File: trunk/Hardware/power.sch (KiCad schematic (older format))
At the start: 131 parts, among them Q1 SI1403, Q2 SI1403, Q3 SI1403, Q4 SI1403, Q5 SI1403, U24 TLV61220, U25 TLV61220, U26 TLV61220, U27 LM3671, U28 DS2710

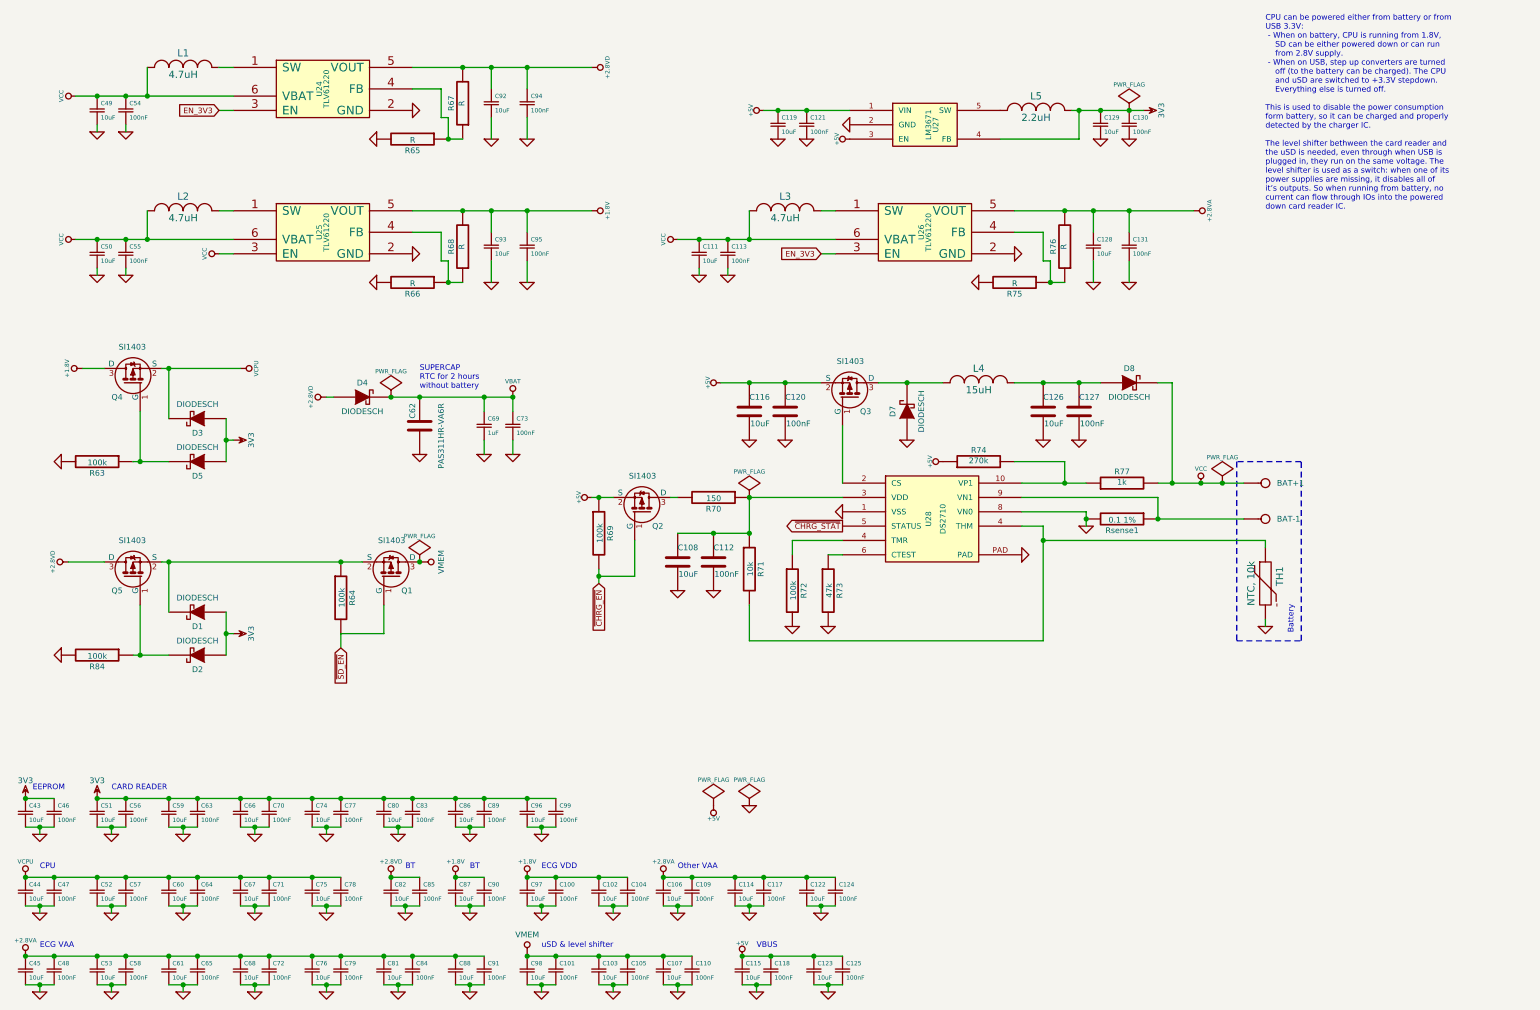
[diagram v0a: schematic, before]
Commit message: Fix even more typos, arrange parts in the schematic.
---
yaml
---
svn_rev: 4
current_ref: refs/heads/master
current_commit: f7ca86bd98997ffeb8958d9e682c09919540c8bc
head_branch: refs/heads/master
migrated_from: 3
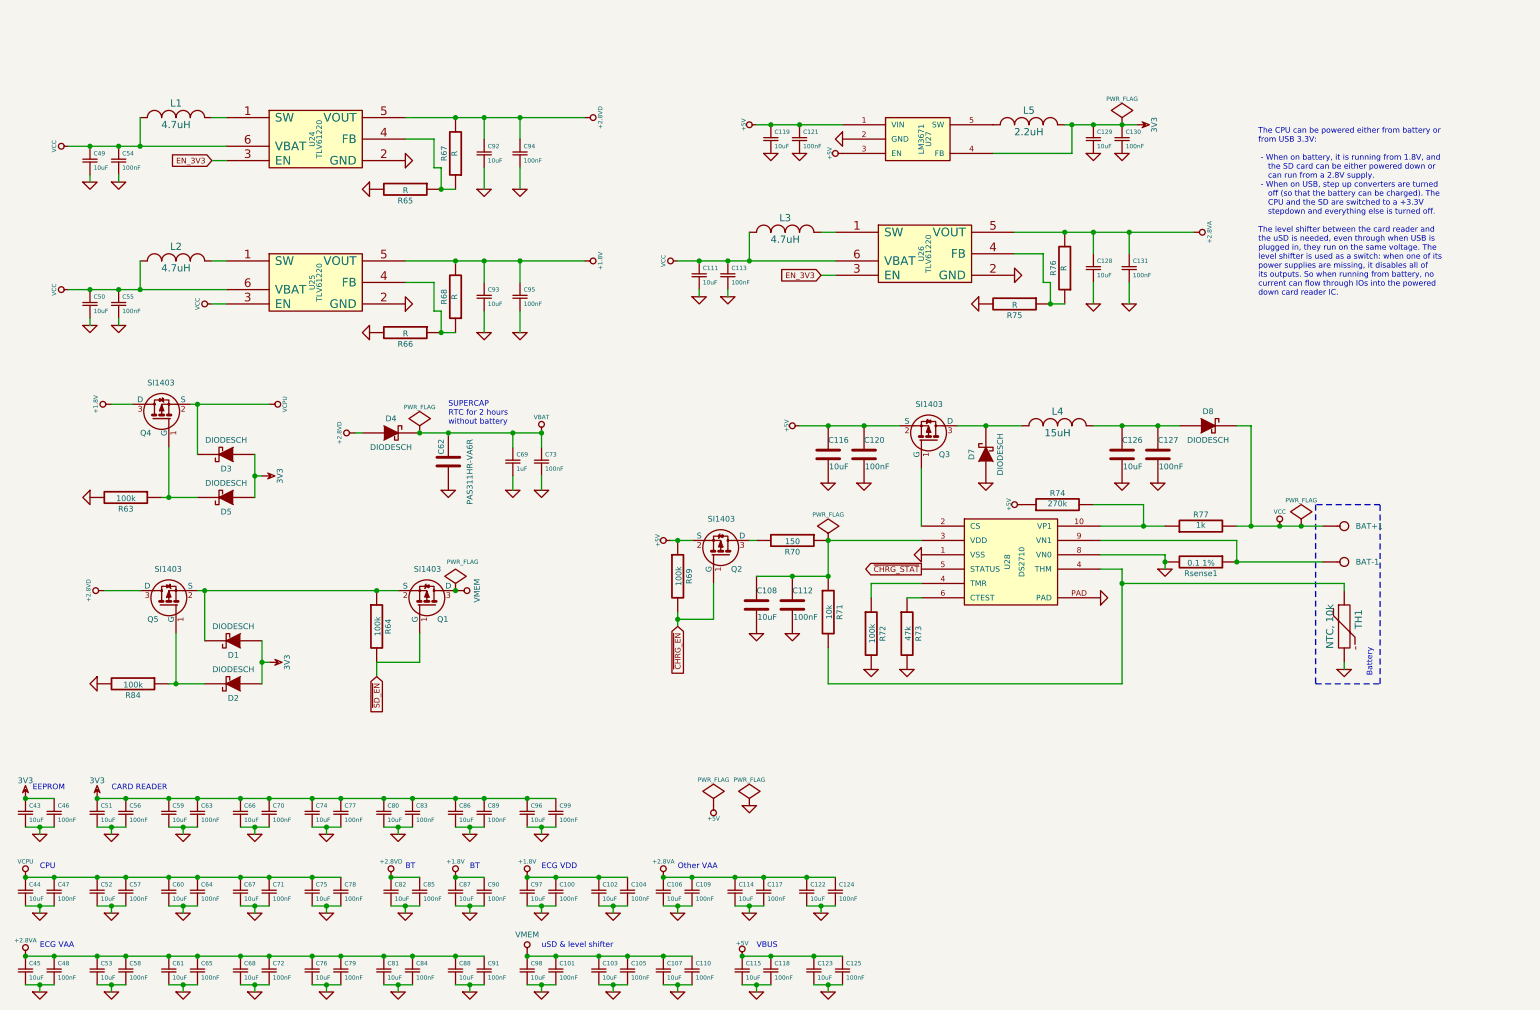
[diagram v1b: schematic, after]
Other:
- note added: "The CPU can be powered either from battery or\nfrom USB 3.3V:\n\n - When on battery, it is running from 1.8V, and\n the SD card can be either powered down or\n can run from a 2.8V supply.\n - When on USB, step up converters are turned\n off (so that the battery can be charged). The\n CPU and the SD are switched to a +3.3V\n stepdown and everything else is turned off.\n\nThe level shifter between 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"
- note removed: "CPU can be powered either from battery or from\nUSB 3.3V:\n - When on battery, CPU is running from 1.8V,\n SD can be either powered down or can run\n from 2.8V supply.\n - When on USB, step up converters are turned\n off (to the battery can be charged). The CPU\n and uSD are switched to +3.3V stepdown.\n Everything else is turned off.\n\nThis is used to disable the power consumption\nform battery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"
- moved on the sheet: BAT+1, BAT-1, C108, C111, C112, C113, C116, C119, C120, C121, C126, C127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

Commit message: Accelerometer connected.
---
yaml
---
svn_rev: 7
current_ref: refs/heads/master
current_commit: ed49ebf97316f3add3e86dbb4995609e667feb0f
head_branch: refs/heads/master
migrated_from: 3
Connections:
- net EN_3V3 renamed EN_2V8
